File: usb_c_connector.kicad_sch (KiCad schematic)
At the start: 24 parts, among them J5 USB_C_Receptacle_USB2.0_16P, J6 USB_C_Receptacle_USB2.0_16P, U6 LM66100DCK, U7 LM66100DCK, U8 USBLC6-2SC6, U9 USBLC6-2SC6

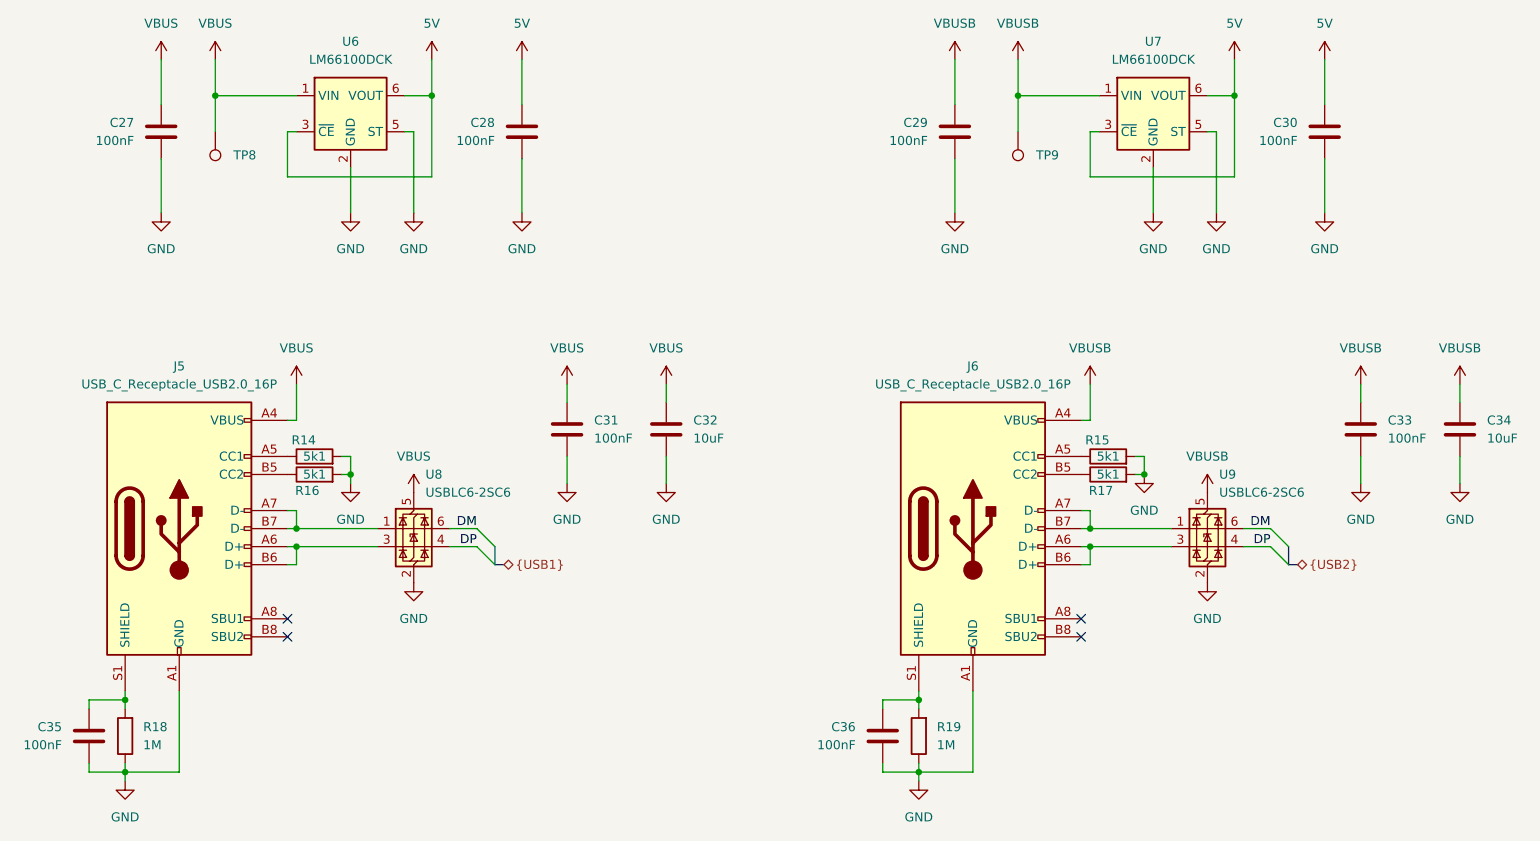
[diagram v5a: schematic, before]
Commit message: Add missing rgb leds
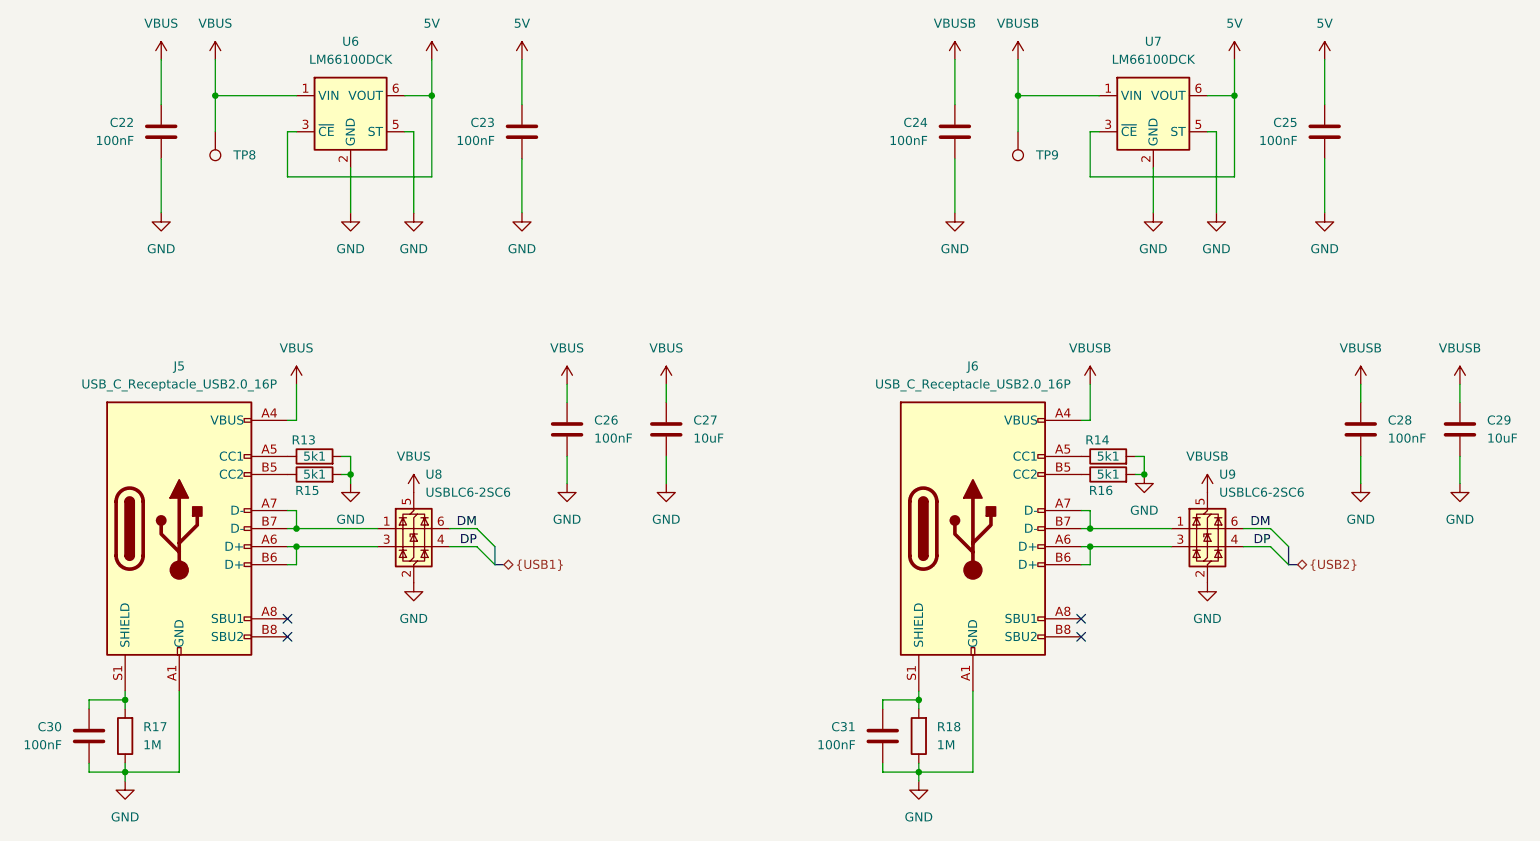
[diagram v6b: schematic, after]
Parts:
- renumbered C27 to C22, C28 to C23, C29 to C24, C30 to C25, C31 to C26, C32 to C27, C33 to C28, C34 to C29, C35 to C30, C36 to C31, R14 to R13, R15 to R14, R16 to R15, R17 to R16, R18 to R17, R19 to R18

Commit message: Replace with cheaper components
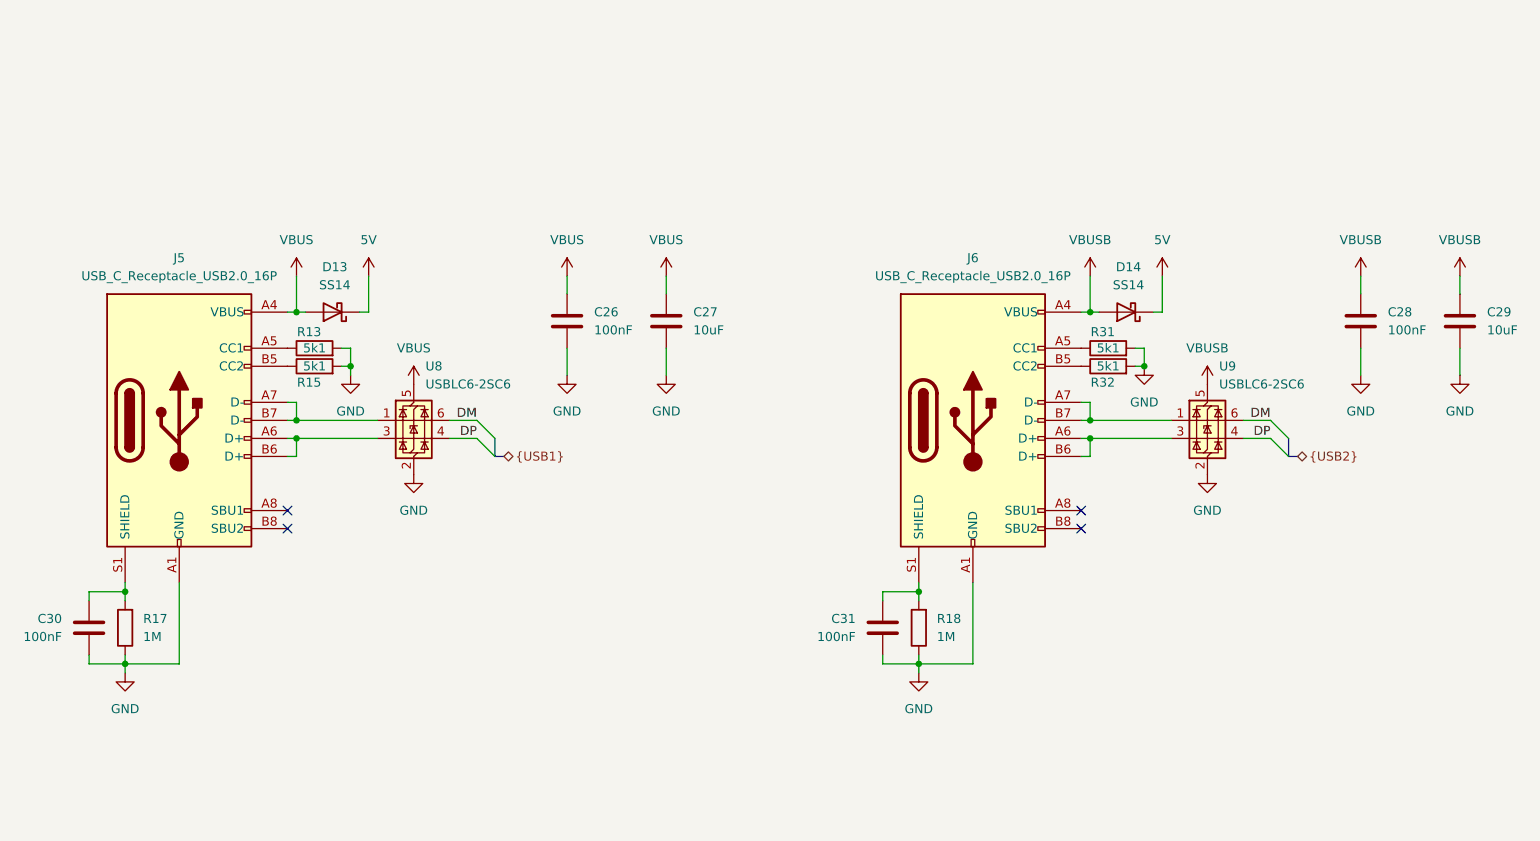
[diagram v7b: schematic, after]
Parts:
- removed C22, C23, C24, C25: 100nF, Capacitor_SMD:C_0603_1608Metric_Pad1.08x0.95mm_HandSolder, symbol Device:C
- removed R14, R16: 5k1, Resistor_SMD:R_0603_1608Metric_Pad0.98x0.95mm_HandSolder, symbol Device:R
- removed TP8, TP9: TestPoint, TestPoint:TestPoint_Pad_D1.5mm, symbol Connector:TestPoint
- removed U6, U7: LM66100DCK, Package_TO_SOT_SMD:SOT-363_SC-70-6, symbol Power_Management:LM66100DCK
- added D13, D14: SS14, Diode_SMD:D_SMA, symbol Diode:SS14
- added R31, R32: 5k1, Resistor_SMD:R_0603_1608Metric_Pad0.98x0.95mm_HandSolder, symbol Device:R
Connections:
- net 5V: now also D13.1 (K), D14.1 (K)
- net GND: now also R31.2, R32.2
- net VBUS: now also D13.2 (A)
- net VBUSB: now also D14.2 (A)
- net at J6.A5 (CC1): now also R31.1
- net at J6.B5 (CC2): now also R32.1
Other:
- moved on the sheet: C26, C27, C28, C29, C30, C31, J5, J6, R13, R15, R17, R18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

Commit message: Delete footprints with no symbol
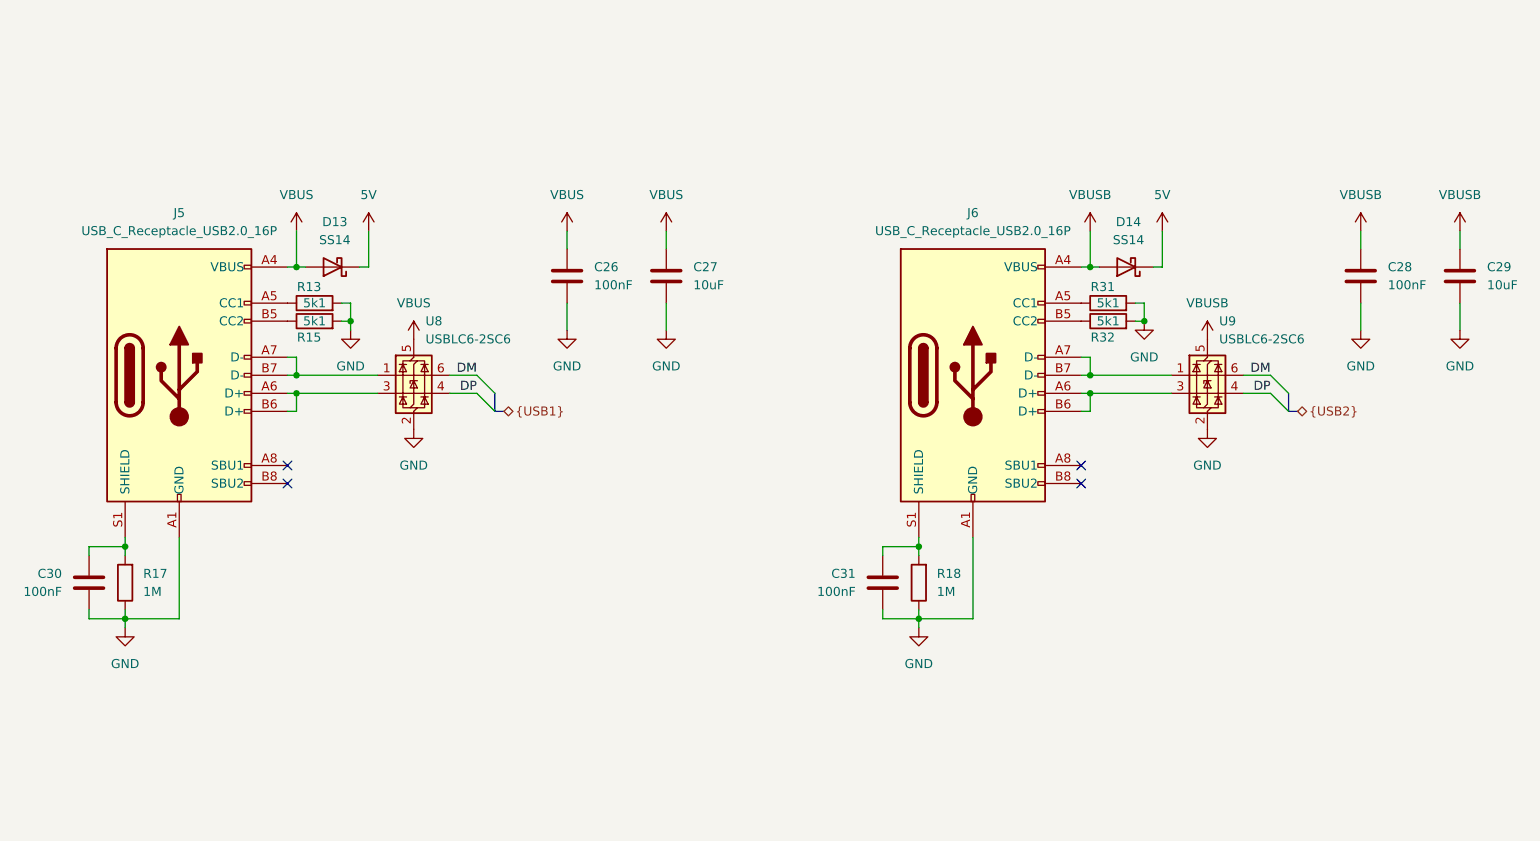
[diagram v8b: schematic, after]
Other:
- moved on the sheet: C26, C27, C28, C29, C30, C31, D13, D14, J5, J6, R13, R15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
